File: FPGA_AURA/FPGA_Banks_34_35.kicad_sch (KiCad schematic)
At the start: 15 parts, among them U1 XC7A35T-2FTG256C

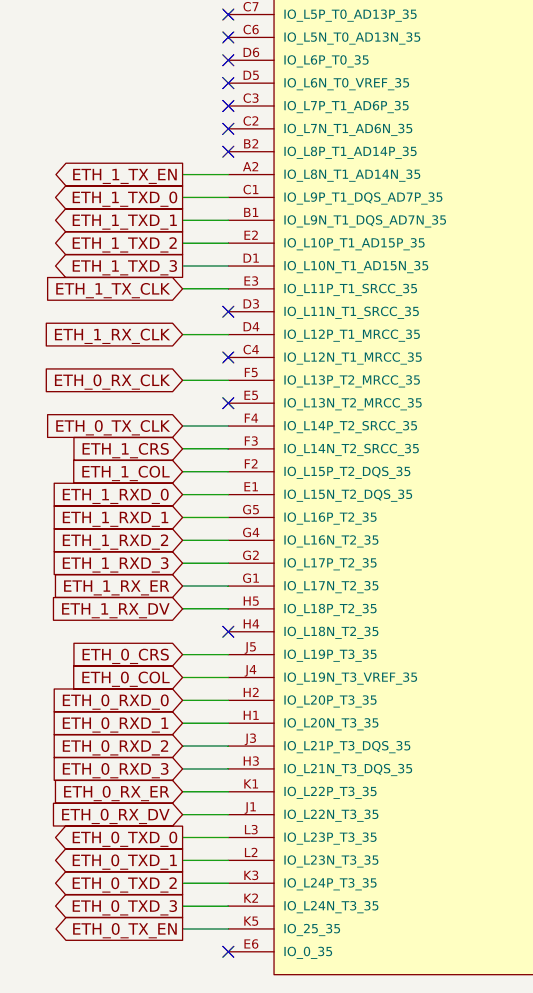
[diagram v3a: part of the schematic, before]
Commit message: All connector pins broken out. Next is QSPI flash, followed by power.
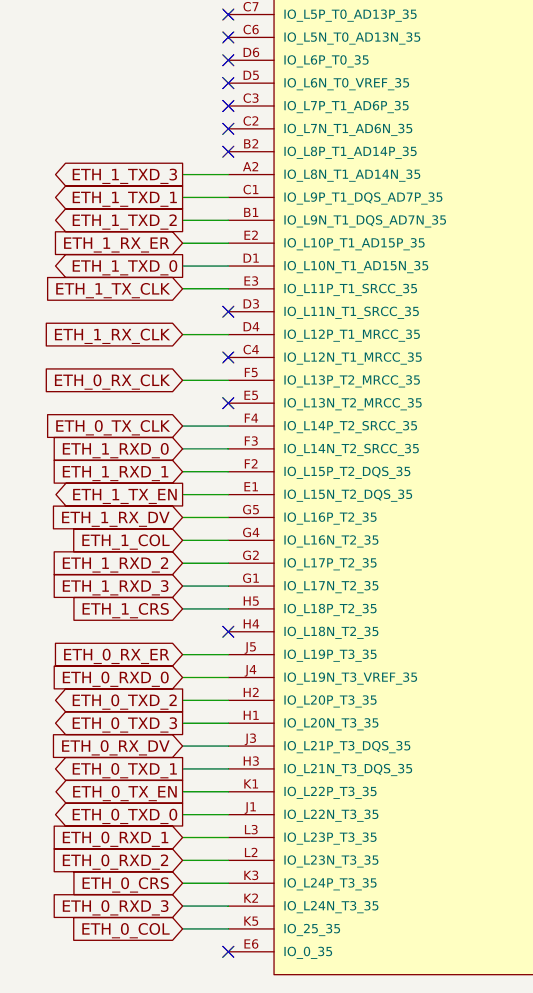
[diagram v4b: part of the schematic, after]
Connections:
- net ETH_0_COL: now also U1.K5 (IO_25_35); no longer U1.J4 (IO_L19N_T3_VREF_35)
- net ETH_0_CRS: now also U1.K3 (IO_L24P_T3_35); no longer U1.J5 (IO_L19P_T3_35)
- net ETH_0_RXD_0: now also U1.J4 (IO_L19N_T3_VREF_35); no longer U1.H2 (IO_L20P_T3_35)
- net ETH_0_RXD_1: now also U1.L3 (IO_L23P_T3_35); no longer U1.H1 (IO_L20N_T3_35)
- net ETH_0_RXD_2: now also U1.L2 (IO_L23N_T3_35); no longer U1.J3 (IO_L21P_T3_DQS_35)
- net ETH_0_RXD_3: now also U1.K2 (IO_L24N_T3_35); no longer U1.H3 (IO_L21N_T3_DQS_35)
- net ETH_0_RX_DV: now also U1.J3 (IO_L21P_T3_DQS_35); no longer U1.J1 (IO_L22N_T3_35)
- net ETH_0_RX_ER: now also U1.J5 (IO_L19P_T3_35); no longer U1.K1 (IO_L22P_T3_35)
- net ETH_0_TXD_0: now also U1.J1 (IO_L22N_T3_35); no longer U1.L3 (IO_L23P_T3_35)
- net ETH_0_TXD_1: now also U1.H3 (IO_L21N_T3_DQS_35); no longer U1.L2 (IO_L23N_T3_35)
- net ETH_0_TXD_2: now also U1.H2 (IO_L20P_T3_35); no longer U1.K3 (IO_L24P_T3_35)
- net ETH_0_TXD_3: now also U1.H1 (IO_L20N_T3_35); no longer U1.K2 (IO_L24N_T3_35)
- net ETH_0_TX_EN: now also U1.K1 (IO_L22P_T3_35); no longer U1.K5 (IO_25_35)
- net ETH_1_COL: now also U1.G4 (IO_L16N_T2_35); no longer U1.F2 (IO_L15P_T2_DQS_35)
- net ETH_1_CRS: now also U1.H5 (IO_L18P_T2_35); no longer U1.F3 (IO_L14N_T2_SRCC_35)
- net ETH_1_RXD_0: now also U1.F3 (IO_L14N_T2_SRCC_35); no longer U1.E1 (IO_L15N_T2_DQS_35)
- net ETH_1_RXD_1: now also U1.F2 (IO_L15P_T2_DQS_35); no longer U1.G5 (IO_L16P_T2_35)
- net ETH_1_RXD_2: now also U1.G2 (IO_L17P_T2_35); no longer U1.G4 (IO_L16N_T2_35)
- net ETH_1_RXD_3: now also U1.G1 (IO_L17N_T2_35); no longer U1.G2 (IO_L17P_T2_35)
- net ETH_1_RX_DV: now also U1.G5 (IO_L16P_T2_35); no longer U1.H5 (IO_L18P_T2_35)
- net ETH_1_RX_ER: now also U1.E2 (IO_L10P_T1_AD15P_35); no longer U1.G1 (IO_L17N_T2_35)
- net ETH_1_TXD_0: now also U1.D1 (IO_L10N_T1_AD15N_35); no longer U1.C1 (IO_L9P_T1_DQS_AD7P_35)
- net ETH_1_TXD_1: now also U1.C1 (IO_L9P_T1_DQS_AD7P_35); no longer U1.B1 (IO_L9N_T1_DQS_AD7N_35)
- net ETH_1_TXD_2: now also U1.B1 (IO_L9N_T1_DQS_AD7N_35); no longer U1.E2 (IO_L10P_T1_AD15P_35)
- net ETH_1_TXD_3: now also U1.A2 (IO_L8N_T1_AD14N_35); no longer U1.D1 (IO_L10N_T1_AD15N_35)
- net ETH_1_TX_EN: now also U1.E1 (IO_L15N_T2_DQS_35); no longer U1.A2 (IO_L8N_T1_AD14N_35)

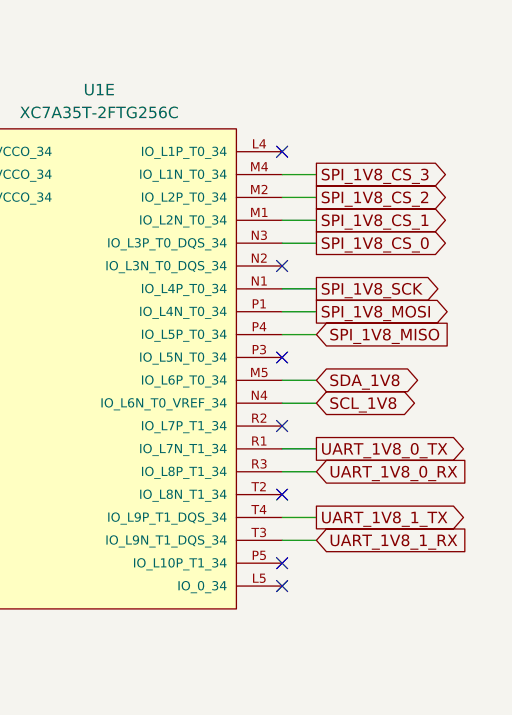
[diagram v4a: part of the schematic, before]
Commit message: Power planes done on layers 3 and 4 as well as almost all mezzanine connections made. QSPI and misc left to do.
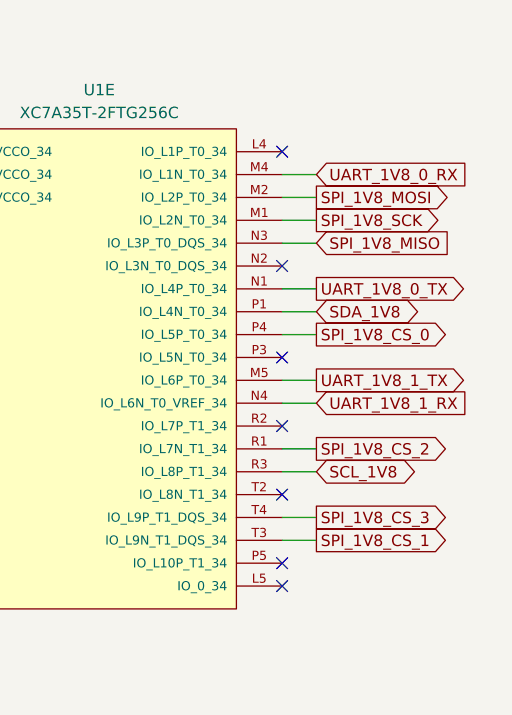
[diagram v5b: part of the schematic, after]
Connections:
- net SCL_1V8: now also U1.R3 (IO_L8P_T1_34); no longer U1.N4 (IO_L6N_T0_VREF_34)
- net SDA_1V8: now also U1.P1 (IO_L4N_T0_34); no longer U1.M5 (IO_L6P_T0_34)
- net SPI_1V8_CS_0: now also U1.P4 (IO_L5P_T0_34); no longer U1.N3 (IO_L3P_T0_DQS_34)
- net SPI_1V8_CS_1: now also U1.T3 (IO_L9N_T1_DQS_34); no longer U1.M1 (IO_L2N_T0_34)
- net SPI_1V8_CS_2: now also U1.R1 (IO_L7N_T1_34); no longer U1.M2 (IO_L2P_T0_34)
- net SPI_1V8_CS_3: now also U1.T4 (IO_L9P_T1_DQS_34); no longer U1.M4 (IO_L1N_T0_34)
- net SPI_1V8_MISO: now also U1.N3 (IO_L3P_T0_DQS_34); no longer U1.P4 (IO_L5P_T0_34)
- net SPI_1V8_MOSI: now also U1.M2 (IO_L2P_T0_34); no longer U1.P1 (IO_L4N_T0_34)
- net SPI_1V8_SCK: now also U1.M1 (IO_L2N_T0_34); no longer U1.N1 (IO_L4P_T0_34)
- net UART_1V8_0_RX: now also U1.M4 (IO_L1N_T0_34); no longer U1.R3 (IO_L8P_T1_34)
- net UART_1V8_0_TX: now also U1.N1 (IO_L4P_T0_34); no longer U1.R1 (IO_L7N_T1_34)
- net UART_1V8_1_RX: now also U1.N4 (IO_L6N_T0_VREF_34); no longer U1.T3 (IO_L9N_T1_DQS_34)
- net UART_1V8_1_TX: now also U1.M5 (IO_L6P_T0_34); no longer U1.T4 (IO_L9P_T1_DQS_34)
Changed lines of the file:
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@@
 	(global_label "UART_1V8_0_TX"
 		(shape output)
-		(at 240.03 113.03 0)
-		(fields_autoplaced yes)
-		(effects
-			(font
-				(size 1.27 1.27)
-			)
-			(justify left)
-		)
-		(property "Intersheetrefs" "${INTERSHEET_REFS}"
-			(at 257.4689 113.03 0)
+		(at 240.03 95.25 0)
+		(fields_autoplaced yes)
+		(effects
+			(font
+				(size 1.27 1.27)
+			)
+			(justify left)
+		)
+		(property "Intersheetrefs" "${INTERSHEET_REFS}"
+			(at 257.4689 95.25 0)
 			(hide yes)
 			(show_name no)
@@
 	(global_label "SPI_1V8_CS_1"
 		(shape output)
-		(at 240.03 87.63 0)
-		(fields_autoplaced yes)
-		(effects
-			(font
-				(size 1.27 1.27)
-			)
-			(justify left)
-		)
-		(property "Intersheetrefs" "${INTERSHEET_REFS}"
-			(at 256.1989 87.63 0)
+		(at 240.03 123.19 0)
+		(fields_autoplaced yes)
+		(effects
+			(font
+				(size 1.27 1.27)
+			)
+			(justify left)
+		)
+		(property "Intersheetrefs" "${INTERSHEET_REFS}"
+			(at 256.1989 123.19 0)
 			(hide yes)
 			(show_name no)
@@
 	(global_label "SPI_1V8_MOSI"
 		(shape output)
-		(at 240.03 97.79 0)
-		(fields_autoplaced yes)
-		(effects
-			(font
-				(size 1.27 1.27)
-			)
-			(justify left)
-		)
-		(property "Intersheetrefs" "${INTERSHEET_REFS}"
-			(at 256.1385 97.79 0)
+		(at 240.03 85.09 0)
+		(fields_autoplaced yes)
+		(effects
+			(font
+				(size 1.27 1.27)
+			)
+			(justify left)
+		)
+		(property "Intersheetrefs" "${INTERSHEET_REFS}"
+			(at 256.1385 85.09 0)
 			(hide yes)
 			(show_name no)
@@
 	(global_label "UART_1V8_0_RX"
 		(shape input)
-		(at 240.03 115.57 0)
-		(fields_autoplaced yes)
-		(effects
-			(font
-				(size 1.27 1.27)
-			)
-			(justify left)
-		)
-		(property "Intersheetrefs" "${INTERSHEET_REFS}"
-			(at 257.7713 115.57 0)
+		(at 240.03 82.55 0)
+		(fields_autoplaced yes)
+		(effects
+			(font
+				(size 1.27 1.27)
+			)
+			(justify left)
+		)
+		(property "Intersheetrefs" "${INTERSHEET_REFS}"
+			(at 257.7713 82.55 0)
 			(hide yes)
 			(show_name no)
@@
 	(global_label "UART_1V8_1_TX"
 		(shape output)
-		(at 240.03 120.65 0)
-		(fields_autoplaced yes)
-		(effects
-			(font
-				(size 1.27 1.27)
-			)
-			(justify left)
-		)
-		(property "Intersheetrefs" "${INTERSHEET_REFS}"
-			(at 257.4689 120.65 0)
+		(at 240.03 105.41 0)
+		(fields_autoplaced yes)
+		(effects
+			(font
+				(size 1.27 1.27)
+			)
+			(justify left)
+		)
+		(property "Intersheetrefs" "${INTERSHEET_REFS}"
+			(at 257.4689 105.41 0)
 			(hide yes)
 			(show_name no)
@@
 	(global_label "UART_1V8_1_RX"
 		(shape input)
-		(at 240.03 123.19 0)
-		(fields_autoplaced yes)
-		(effects
-			(font
-				(size 1.27 1.27)
-			)
-			(justify left)
-		)
-		(property "Intersheetrefs" "${INTERSHEET_REFS}"
-			(at 257.7713 123.19 0)
+		(at 240.03 107.95 0)
+		(fields_autoplaced yes)
+		(effects
+			(font
+				(size 1.27 1.27)
+			)
+			(justify left)
+		)
+		(property "Intersheetrefs" "${INTERSHEET_REFS}"
+			(at 257.7713 107.95 0)
 			(hide yes)
 			(show_name no)
@@
 	(global_label "SCL_1V8"
 		(shape bidirectional)
-		(at 240.03 107.95 0)
-		(fields_autoplaced yes)
-		(effects
-			(font
-				(size 1.27 1.27)
-			)
-			(justify left)
-		)
-		(property "Intersheetrefs" "${INTERSHEET_REFS}"
-			(at 252.1093 107.95 0)
+		(at 240.03 115.57 0)
+		(fields_autoplaced yes)
+		(effects
+			(font
+				(size 1.27 1.27)
+			)
+			(justify left)
+		)
+		(property "Intersheetrefs" "${INTERSHEET_REFS}"
+			(at 252.1093 115.57 0)
 			(hide yes)
 			(show_name no)
@@
 	(global_label "SPI_1V8_CS_2"
 		(shape output)
-		(at 240.03 85.09 0)
-		(fields_autoplaced yes)
-		(effects
-			(font
-				(size 1.27 1.27)
-			)
-			(justify left)
-		)
-		(property "Intersheetrefs" "${INTERSHEET_REFS}"
-			(at 256.1989 85.09 0)
+		(at 240.03 113.03 0)
+		(fields_autoplaced yes)
+		(effects
+			(font
+				(size 1.27 1.27)
+			)
+			(justify left)
+		)
+		(property "Intersheetrefs" "${INTERSHEET_REFS}"
+			(at 256.1989 113.03 0)
 			(hide yes)
 			(show_name no)
@@
 	(global_label "SPI_1V8_CS_3"
 		(shape output)
-		(at 240.03 82.55 0)
-		(fields_autoplaced yes)
-		(effects
-			(font
-				(size 1.27 1.27)
-			)
-			(justify left)
-		)
-		(property "Intersheetrefs" "${INTERSHEET_REFS}"
-			(at 256.1989 82.55 0)
+		(at 240.03 120.65 0)
+		(fields_autoplaced yes)
+		(effects
+			(font
+				(size 1.27 1.27)
+			)
+			(justify left)
+		)
+		(property "Intersheetrefs" "${INTERSHEET_REFS}"
+			(at 256.1989 120.65 0)
 			(hide yes)
 			(show_name no)
@@
 	(global_label "SPI_1V8_SCK"
 		(shape output)
-		(at 240.03 95.25 0)
-		(fields_autoplaced yes)
-		(effects
-			(font
-				(size 1.27 1.27)
-			)
-			(justify left)
-		)
-		(property "Intersheetrefs" "${INTERSHEET_REFS}"
-			(at 255.2918 95.25 0)
+		(at 240.03 87.63 0)
+		(fields_autoplaced yes)
+		(effects
+			(font
+				(size 1.27 1.27)
+			)
+			(justify left)
+		)
+		(property "Intersheetrefs" "${INTERSHEET_REFS}"
+			(at 255.2918 87.63 0)
 			(hide yes)
 			(show_name no)
@@
 	(global_label "SPI_1V8_CS_0"
 		(shape output)
-		(at 240.03 90.17 0)
-		(fields_autoplaced yes)
-		(effects
-			(font
-				(size 1.27 1.27)
-			)
-			(justify left)
-		)
-		(property "Intersheetrefs" "${INTERSHEET_REFS}"
-			(at 256.1989 90.17 0)
+		(at 240.03 100.33 0)
+		(fields_autoplaced yes)
+		(effects
+			(font
+				(size 1.27 1.27)
+			)
+			(justify left)
+		)
+		(property "Intersheetrefs" "${INTERSHEET_REFS}"
+			(at 256.1989 100.33 0)
 			(hide yes)
 			(show_name no)
@@
 	(global_label "SDA_1V8"
 		(shape bidirectional)
-		(at 240.03 105.41 0)
-		(fields_autoplaced yes)
-		(effects
-			(font
-				(size 1.27 1.27)
-			)
-			(justify left)
-		)
-		(property "Intersheetrefs" "${INTERSHEET_REFS}"
-			(at 252.1698 105.41 0)
+		(at 240.03 97.79 0)
+		(fields_autoplaced yes)
+		(effects
+			(font
+				(size 1.27 1.27)
+			)
+			(justify left)
+		)
+		(property "Intersheetrefs" "${INTERSHEET_REFS}"
+			(at 252.1698 97.79 0)
 			(hide yes)
 			(show_name no)
@@
 	(global_label "SPI_1V8_MISO"
 		(shape input)
-		(at 240.03 100.33 0)
-		(fields_autoplaced yes)
-		(effects
-			(font
-				(size 1.27 1.27)
-			)
-			(justify left)
-		)
-		(property "Intersheetrefs" "${INTERSHEET_REFS}"
-			(at 256.1385 100.33 0)
-			(hide yes)
-			(show_name no)
+		(at 240.03 90.17 0)
+		(fields_autoplaced yes)
+		(effects
+			(font
+				(size 1.27 1.27)
+			)
+			(justify left)
+		)
+		(property "Intersheetrefs" "${INTERSHEET_REFS}"
+			(at 256.1385 90.17 0)
+			(hide yes)
+			(show_name no)

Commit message: Continued routing and pin swapping, 11 nets left to route.
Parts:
- added R600: 10k, Resistor_SMD:R_0402_1005Metric, symbol Device:R
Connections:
- net +1V8: now also R600.1
- net SYS_nRST: now reaches U1.T2 (IO_L8N_T1_34)
- net SYS_nRST: now also R600.2
- no-connect marks 23 -> 22
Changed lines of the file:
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@@
 	)
 	(junction
+		(at 262.89 118.11)
+		(diameter 0)
+		(color 0 0 0 0)
+	)
+	(junction
 		(at 104.14 57.15)
 		(diameter 0)
@@
 	)
 	(no_connect
-		(at 236.22 118.11)
-	)
-	(no_connect
 		(at 236.22 128.27)
 	)
@@
 	(wire
 		(pts
+			(xy 236.22 118.11) (xy 262.89 118.11)
+		)
+		(stroke
+			(width 0)
+			(type default)
+		)
+	)
+	(wire
+		(pts
 			(xy 104.14 57.15) (xy 104.14 59.69)
 		)
@@
 	(wire
 		(pts
+			(xy 262.89 116.84) (xy 262.89 118.11)
+		)
+		(stroke
+			(width 0)
+			(type default)
+		)
+	)
+	(wire
+		(pts
 			(xy 57.15 49.53) (xy 52.07 49.53)
 		)
@@
 	(wire
 		(pts
+			(xy 262.89 107.95) (xy 262.89 109.22)
+		)
+		(stroke
+			(width 0)
+			(type default)
+		)
+	)
+	(wire
+		(pts
 			(xy 186.69 125.73) (xy 186.69 127)
 		)
@@
 	(wire
 		(pts
+			(xy 264.16 118.11) (xy 262.89 118.11)
+		)
+		(stroke
+			(width 0)
+			(type default)
+		)
+	)
+	(wire
+		(pts
 			(xy 162.56 105.41) (xy 162.56 106.68)
 		)
@@
 		)
 	)
+	(global_label "SYS_nRST"
+		(shape output)
+		(at 264.16 118.11 0)
+		(fields_autoplaced yes)
+		(effects
+			(font
+				(size 1.27 1.27)
+			)
+			(justify left)
+		)
+		(property "Intersheetrefs" "${INTERSHEET_REFS}"
+			(at 276.2165 118.11 0)
+			(hide yes)
+			(show_name no)
+			(do_not_autoplace no)
+			(effects
+				(font
+					(size 1.27 1.27)
+				)
+				(justify left)
+			)
+		)
+	)
 	(global_label "ETH_0_TXD_2"
 		(shape output)
@@
 	)
 	(symbol
+		(lib_id "power:+1V8")
+		(at 262.89 107.95 0)
+		(mirror y)
+		(unit 1)
+		(body_style 1)
+		(exclude_from_sim no)
+		(in_bom yes)
+		(on_board yes)
+		(in_pos_files yes)
+		(dnp no)
+		(fields_autoplaced yes)
+		(property "Reference" "#PWR045"
+			(at 262.89 111.76 0)
+			(hide yes)
+			(show_name no)
+			(do_not_autoplace no)
+			(effects
+				(font
+					(size 1.27 1.27)
+				)
+			)
+		)
+		(property "Value" "+1V8"
+			(at 262.89 102.87 0)
+			(show_name no)
+			(do_not_autoplace no)
+			(effects
+				(font
+					(size 1.27 1.27)
+				)
+			)
+		)
+		(property "Footprint" ""
+			(at 262.89 107.95 0)
+			(hide yes)
+			(show_name no)
+			(do_not_autoplace no)
+			(effects
+				(font
+					(size 1.27 1.27)
+				)
+			)
+		)
+		(property "Datasheet" ""
+			(at 262.89 107.95 0)
+			(hide yes)
+			(show_name no)
+			(do_not_autoplace no)
+			(effects
+				(font
+					(size 1.27 1.27)
+				)
+			)
+		)
+		(property "Description" "Power symbol creates a global label with name \"+1V8\""
+			(at 262.89 107.95 0)
+			(hide yes)
+			(show_name no)
+			(do_not_autoplace no)
+			(effects
+				(font
+					(size 1.27 1.27)
+				)
+			)
+		)
+		(pin "1"
+		)
+		(instances
+			(project "FPGA_AURA"
+				(path "/3d83cb23-9528-4d06-8969-599520e9eb23/2d3446c8-405c-4eaf-9ac6-0e0b69b3b124"
+					(reference "#PWR045")
+					(unit 1)
+				)
+			)
+		)
+	)
+	(symbol
 		(lib_id "power:GND")
 		(at 175.26 106.68 0)
@@
 					(unit 1)
 				)
+			)
+		)
+	)
+	(symbol
+		(lib_id "Device:R")
+		(at 262.89 113.03 0)
+		(mirror y)
+		(unit 1)
+		(body_style 1)
+		(exclude_from_sim no)
+		(in_bom yes)
+		(on_board yes)
+		(in_pos_files yes)
+		(dnp no)
+		(fields_autoplaced yes)
+		(property "Reference" "R600"
+			(at 265.43 111.7599 0)
+			(show_name no)
+			(do_not_autoplace no)
+			(effects
+				(font
+					(size 1.27 1.27)
+				)
+				(justify right)
+			)
+		)
+		(property "Value" "10k"
+			(at 265.43 114.2999 0)
+			(show_name no)
+			(do_not_autoplace no)
+			(effects
+				(font
+					(size 1.27 1.27)
+				)
+				(justify right)
+			)
+		)
+		(property "Footprint" "Resistor_SMD:R_0402_1005Metric"
+			(at 264.668 113.03 90)
+			(hide yes)
+			(show_name no)
+			(do_not_autoplace no)
+			(effects
+				(font
+					(size 1.27 1.27)
+				)
+			)
+		)
+		(property "Datasheet" ""
+			(at 262.89 113.03 0)
+			(hide yes)
+			(show_name no)
+			(do_not_autoplace no)
+			(effects
+				(font
+					(size 1.27 1.27)
+				)
+			)
+		)
+		(property "Description" "Resistor"
+			(at 262.89 113.03 0)
+			(hide yes)
+			(show_name no)
+			(do_not_autoplace no)
+			(effects
+				(font
+					(size 1.27 1.27)
+				)
+			)
+		)
+		(pin "2"
+		)
+		(pin "1"
+		)
+		(instances
+			(project "FPGA_AURA"
+				(path "/3d83cb23-9528-4d06-8969-599520e9eb23/2d3446c8-405c-4eaf-9ac6-0e0b69b3b124"
+					(reference "R600")
+					(unit 1)
+				)
